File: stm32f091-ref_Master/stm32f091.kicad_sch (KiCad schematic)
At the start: 62 parts, among them J1 Conn_02x05_Odd_Even, J2 Conn_01x09_Female, J3 Conn_01x08_Female, J4 Conn_01x02_Female, SW1 SW_Push, U1 LD1117S33TR_SOT223, U2 LM324, U3 STM32F091RCTx, U4 LM386

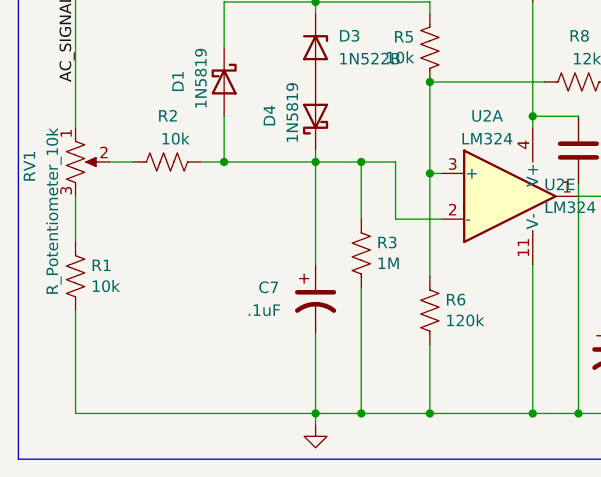
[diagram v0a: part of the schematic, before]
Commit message: new pcb with the traces
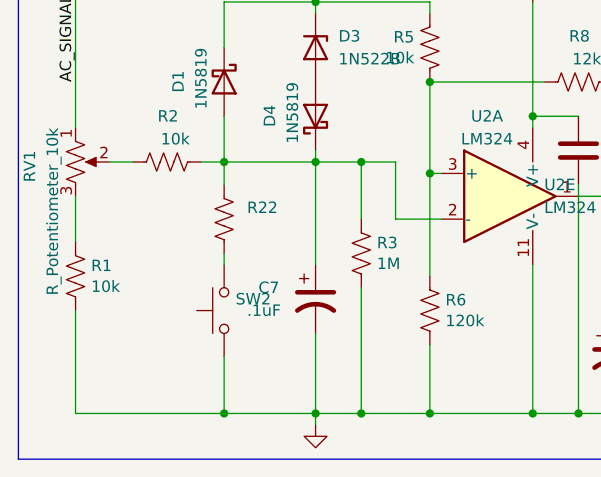
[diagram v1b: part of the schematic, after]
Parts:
- added R22: (no value), symbol Device:R_US
- added SW2: (no value), symbol Switch:SW_Push
- C1, C10, C11, C12, C13, C14, C15, C16, C17, C19, C2, C20, C21, C3, C4, C5, C6, C7, C8, C9: footprint (none) -> Capacitor_SMD:C_0805_2012Metric_Pad1.18x1.45mm_HandSolder
- R1, R10, R11, R12, R13, R14, R15, R16, R17, R18, R19, R2, R20, R21, R3, R4, R5, R6, R7, R8, R9: footprint (none) -> Resistor_SMD:R_0805_2012Metric_Pad1.20x1.40mm_HandSolder
- SW1: footprint (none) -> Button_Switch_SMD:SW_SPST_PTS645
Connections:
- net GND: now also SW2.1
- net at C7.1, D1.2 (A), D4.1 (K)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: now also R22.1
- new net: R22.2, SW2.2

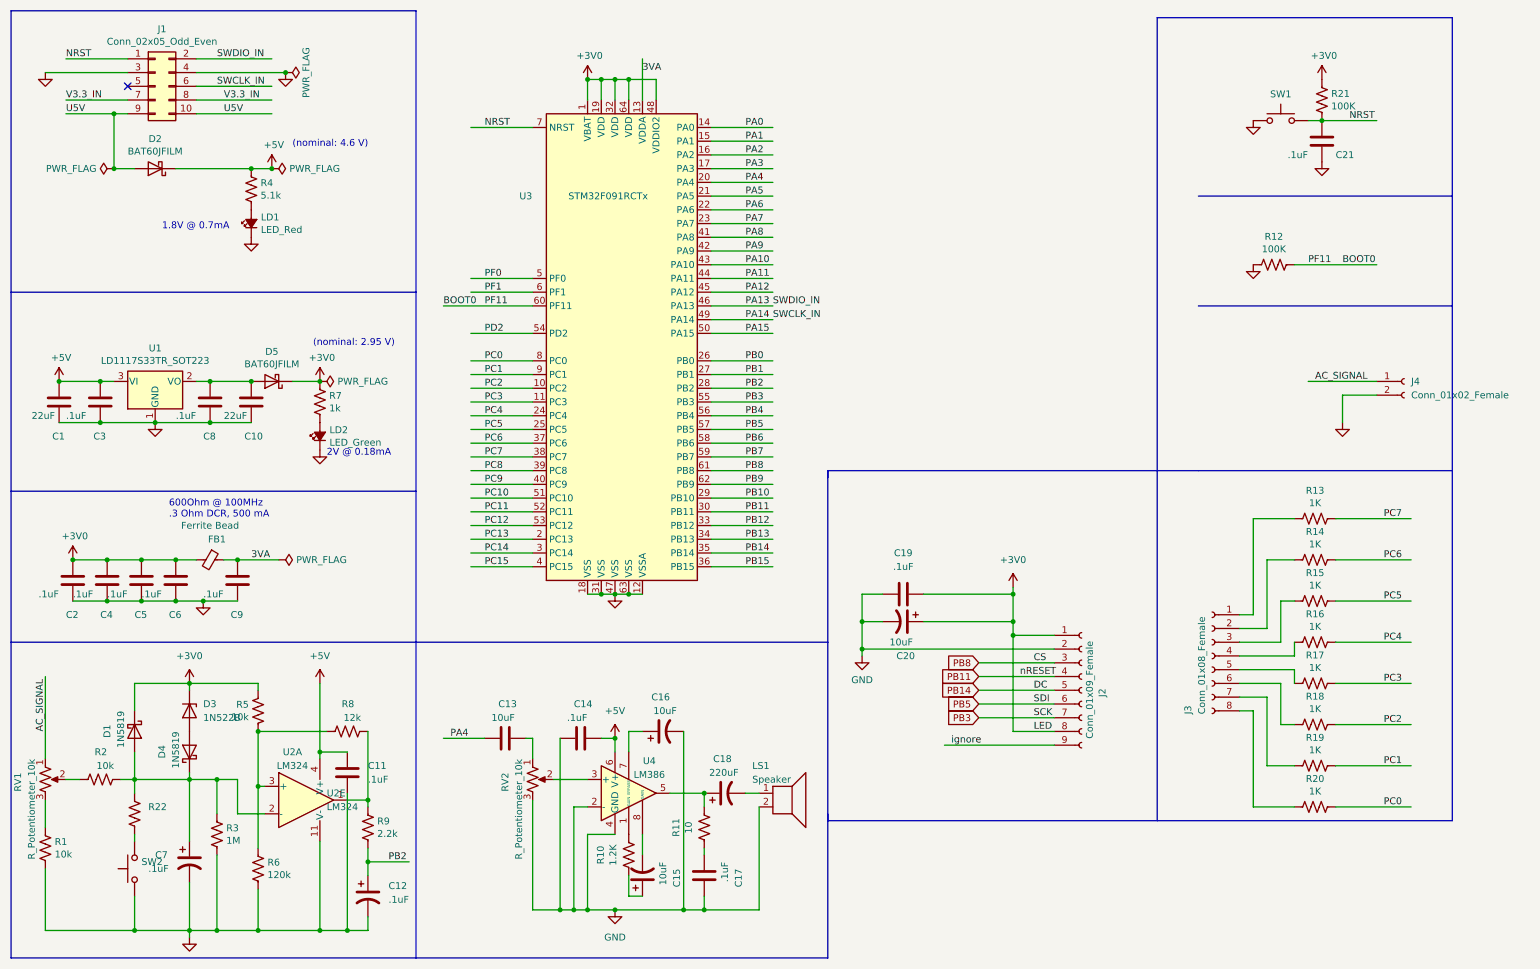
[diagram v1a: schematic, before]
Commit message: schematic and netlist with AC-DC circuits added
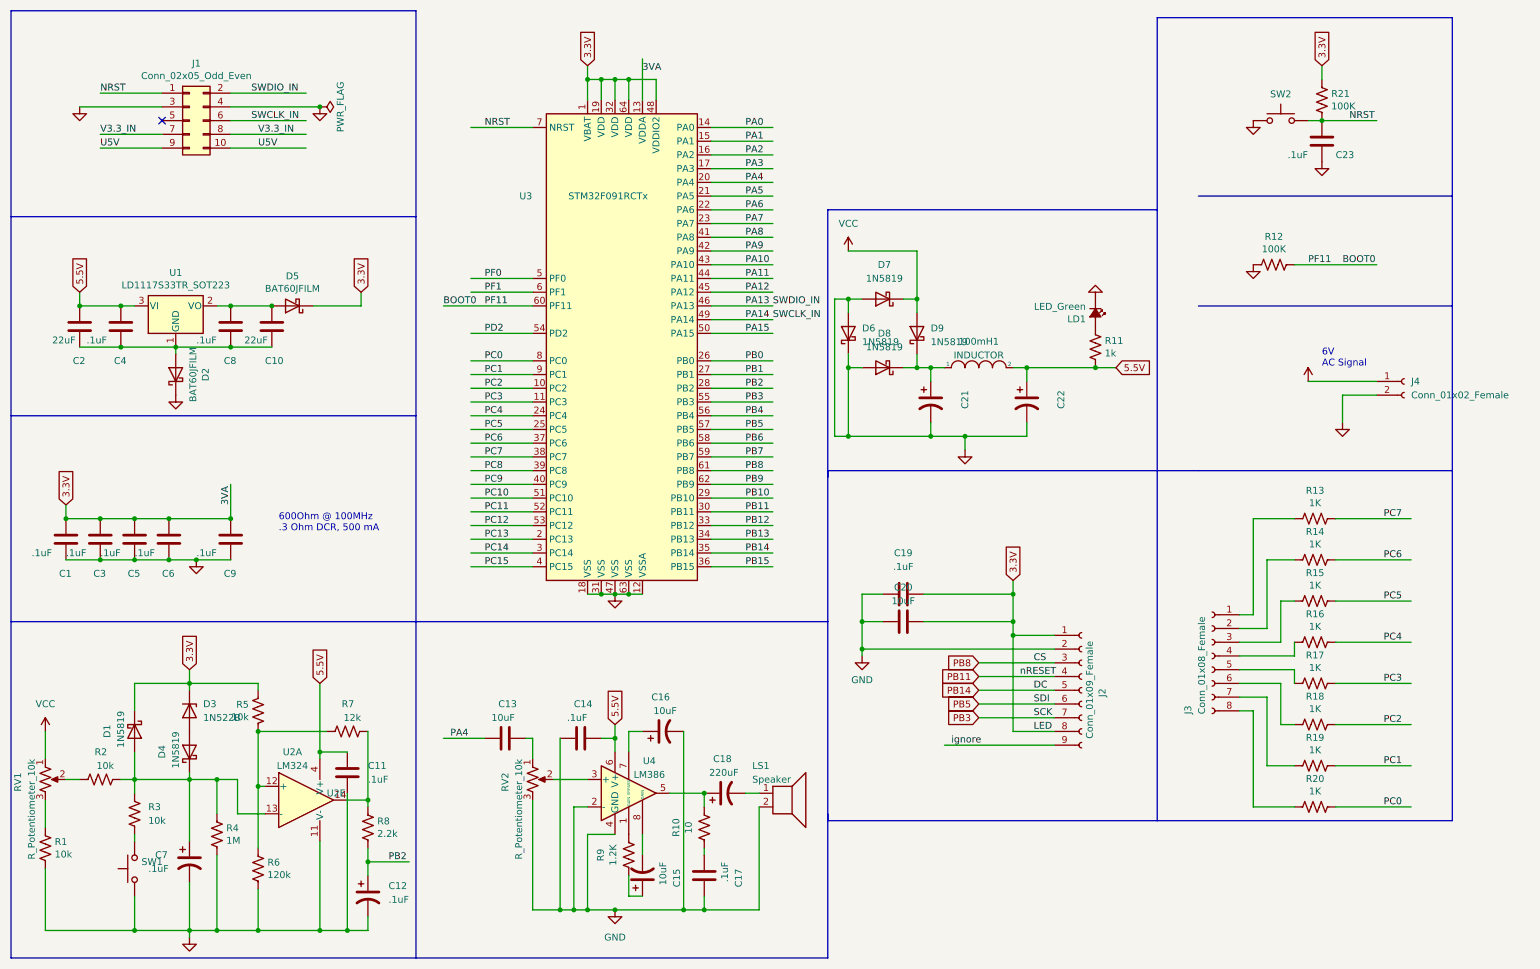
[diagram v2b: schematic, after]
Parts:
- removed C20: 10uF, Capacitor_SMD:C_0805_2012Metric_Pad1.18x1.45mm_HandSolder, symbol Device:C_Polarized_US
- removed FB1: Ferrite Bead, Inductor_SMD:L_0805_2012Metric_Pad1.15x1.40mm_HandSolder, symbol stm32f091-rescue:Ferrite_Bead_Small-Device
- removed LD2: LED_Green, LED_THT:LED_D2.0mm_W4.8mm_H2.5mm_FlatTop, symbol stm32f091-rescue:LED_Small_ALT-Device
- removed R4: 5.1k, Resistor_SMD:R_0805_2012Metric_Pad1.20x1.40mm_HandSolder, symbol Device:R_US
- removed R7: 1k, Resistor_SMD:R_0805_2012Metric_Pad1.20x1.40mm_HandSolder, symbol Device:R_US
- added 100mH1: INDUCTOR, symbol pspice:INDUCTOR
- added C20: 10uF, Capacitor_SMD:C_0805_2012Metric_Pad1.18x1.45mm_HandSolder, symbol pspice:C
- added C21, C22: (no value), symbol Device:C_Polarized_US
- added D6, D7, D8, D9: 1N5819, Diode_THT:D_DO-41_SOD81_P10.16mm_Horizontal, symbol Diode:1N5819
- added R11: 1k, Resistor_SMD:R_0805_2012Metric_Pad1.20x1.40mm_HandSolder, symbol Device:R_US
- C18: footprint (none) -> Capacitor_THT:CP_Radial_D10.0mm_P5.00mm
- D3: footprint Diode_THT:D_DO-201_P15.24mm_Horizontal -> (none)
- LD1: value LED_Red -> LED_Green
- R3: renamed from R22; value (none) -> 10k; footprint (none) -> Resistor_SMD:R_0805_2012Metric_Pad1.20x1.40mm_HandSolder
- U2: value LM324 -> (none); footprint local_models:U2 -> (none)
- renumbered C2 to C1, C1 to C2, C21 to C23, C4 to C3, C3 to C4, R11 to R10, R3 to R4, R8 to R7, R9 to R8, R10 to R9, SW2 to SW1, SW1 to SW2
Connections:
- net 3VA is gone; now on net 3.3V: C9.1, U3.13 (VDDA)
- net GND: now also D2.1 (K), C20.2, C21.2, C22.2, D6.1 (K), D6.2 (A), D7.2 (A), D8.2 (A); no longer C10.2, C2.2, C4.2, C8.2, U1.1 (GND)
- net U5V: no longer D2.2 (A)
- net at LD1.2 (A): now also R11.1
- net at C7.1, D1.2 (A), D4.1 (K)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: now also U2.13 (-); no longer U2.2 (-)
- net at R7.2, R8.1: now also U2.14; no longer U2.1
- net at R5.2, R6.1, R7.1: now also U2.12 (+); no longer U2.3 (+)
- net +3V0 renamed 3.3V
- net 3.3V: now also C20.1
- net +5V renamed 5.5V
- net 5.5V: now also 100mH1.2, C22.1, R11.2; no longer D2.1 (K)
- net AC_SIGNAL renamed VCC
- net VCC: now also D7.1 (K), D9.2 (A)
- new net: C10.2, C2.2, C4.2, C8.2, D2.2 (A), U1.1 (GND)
- new net: 100mH1.1, C21.1, D8.1 (K), D9.1 (K)
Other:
- note added: "6V AC Signal"
- note removed: "(nominal: 2.95 V)"
- note removed: "(nominal: 4.6 V)"
- note removed: "1.8V @ 0.7mA"
- note removed: "2V @ 0.18mA"
- moved on the sheet: C1, C10, C2, C3, C4, C5, C6, C8, C9, D5, J1, U1

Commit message: rick's changes, still need to swap out ic footprints
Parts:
- 100mH1: footprint (none) -> Inductor_THT:L_Radial_D10.0mm_P5.00mm_Neosid_SD12_style3
- C21, C22: value (none) -> 100uF; footprint (none) -> Capacitor_THT:CP_Radial_D10.0mm_P5.00mm
- D3: footprint (none) -> Diode_THT:D_DO-41_SOD81_P10.16mm_Horizontal
- SW1: value (none) -> SW_Push; footprint (none) -> Button_Switch_SMD:SW_SPST_PTS645
- U2: value (none) -> LM324; footprint (none) -> local_models:U2
- U4: footprint local_models:U4 -> (none)
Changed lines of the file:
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@@
       (effects (font (size 1.27 1.27)) (justify left))
     )
-    (property "Value" "" (id 1) (at 73.66 161.2899 0)
-      (effects (font (size 1.27 1.27)) (justify left))
-    )
-    (property "Footprint" "" (id 2) (at 73.66 157.48 0)
+    (property "Value" "LM324" (id 1) (at 73.66 161.2899 0)
+      (effects (font (size 1.27 1.27)) (justify left))
+    )
+    (property "Footprint" "local_models:U2" (id 2) (at 73.66 157.48 0)
       (effects (font (size 1.27 1.27)) hide)
     )
@@
     (property "Reference" "100mH1" (id 0) (at 194.31 75.1672 0))
     (property "Value" "INDUCTOR" (id 1) (at 194.31 77.7041 0))
-    (property "Footprint" "" (id 2) (at 194.31 80.01 0)
+    (property "Footprint" "Inductor_THT:L_Radial_D10.0mm_P5.00mm_Neosid_SD12_style3" (id 2) (at 194.31 80.01 0)
       (effects (font (size 1.27 1.27)) hide)
     )
@@
       (effects (font (size 1.27 1.27)) (justify right))
     )
-    (property "Value" "" (id 1) (at 39.37 173.9899 90)
+    (property "Value" "SW_Push" (id 1) (at 39.37 173.9899 90)
       (effects (font (size 1.27 1.27)) (justify right))
     )
-    (property "Footprint" "" (id 2) (at 33.02 172.72 0)
+    (property "Footprint" "Button_Switch_SMD:SW_SPST_PTS645" (id 2) (at 33.02 172.72 0)
       (effects (font (size 1.27 1.27)) hide)
     )
@@
     (property "Reference" "U4" (id 0) (at 133.35 152.781 0))
     (property "Value" "LM386" (id 1) (at 133.35 155.321 0))
-    (property "Footprint" "local_models:U4" (id 2) (at 132.08 156.21 0)
+    (property "Footprint" "" (id 2) (at 132.08 156.21 0)
       (effects (font (size 1.27 1.27)) hide)
     )
@@
       (effects (font (size 1.27 1.27)) (justify left))
     )
-    (property "Value" "" (id 1) (at 189.23 88.9 90)
-      (effects (font (size 1.27 1.27)) (justify left))
-    )
-    (property "Footprint" "" (id 2) (at 185.42 86.36 0)
+    (property "Value" "100uF" (id 1) (at 189.23 88.9 90)
+      (effects (font (size 1.27 1.27)) (justify left))
+    )
+    (property "Footprint" "Capacitor_THT:CP_Radial_D10.0mm_P5.00mm" (id 2) (at 185.42 86.36 0)
       (effects (font (size 1.27 1.27)) hide)
     )
@@
       (effects (font (size 1.27 1.27)) hide)
     )
+    (pin "12")
+    (pin "13")
     (pin "14")
-    (pin "13")
-    (pin "12")
     (pin "5")
     (pin "6")
@@
       (effects (font (size 1.27 1.27)) (justify left))
     )
-    (property "Footprint" "" (id 2) (at 48.26 139.065 0)
+    (property "Footprint" "Diode_THT:D_DO-41_SOD81_P10.16mm_Horizontal" (id 2) (at 48.26 139.065 0)
       (effects (font (size 1.27 1.27)) hide)
     )
@@
       (effects (font (size 1.27 1.27)) (justify left))
     )
-    (property "Value" "" (id 1) (at 207.01 88.9 90)
-      (effects (font (size 1.27 1.27)) (justify left))
-    )
-    (property "Footprint" "" (id 2) (at 203.2 86.36 0)
+    (property "Value" "100uF" (id 1) (at 207.01 88.9 90)
+      (effects (font (size 1.27 1.27)) (justify left))
+    )
+    (property "Footprint" "Capacitor_THT:CP_Radial_D10.0mm_P5.00mm" (id 2) (at 203.2 86.36 0)
       (effects (font (size 1.27 1.27)) hide)
     )
@@
       (effects (font (size 1.27 1.27)) hide)
     )
-    (property "Value" "" (id 1) (at 255.27 77.47 0))
+    (property "Value" "VCC" (id 1) (at 255.27 77.47 0))
     (property "Footprint" "" (id 2) (at 255.27 82.55 0)
       (effects (font (size 1.27 1.27)) hide)
@@
     )
     (path "/7f7682d1-a5f5-4493-8e01-c35882b526c9"
-      (reference "U4") (unit 1) (value "LM386") (footprint "local_models:U4")
-    )
-  )
+      (reference "U4") (unit 1) (value "LM386") (footprint "Package_DIP:DIP-8_W7.62mm")
+    )
+  )
